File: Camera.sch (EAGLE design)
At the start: 49 parts, among them J1 DM3AT-SF-PEJM5, SW5 THAU13-AB-R, SW6 THAU13-AB-R, SW7 TVAF06-A020B-R, SW8 TVAF06-A020B-R, U4 OPA340N, U5 DRIVER-LV8548MC-AH(SOIC10), U6 I-02247_NJM2845

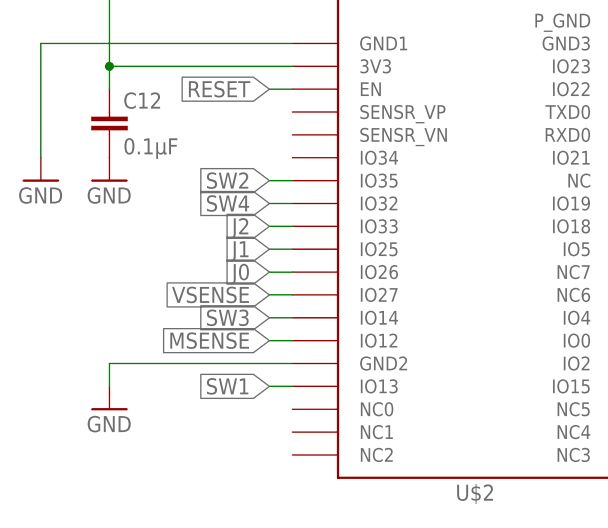
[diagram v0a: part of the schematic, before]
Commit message: Fix analog input pins
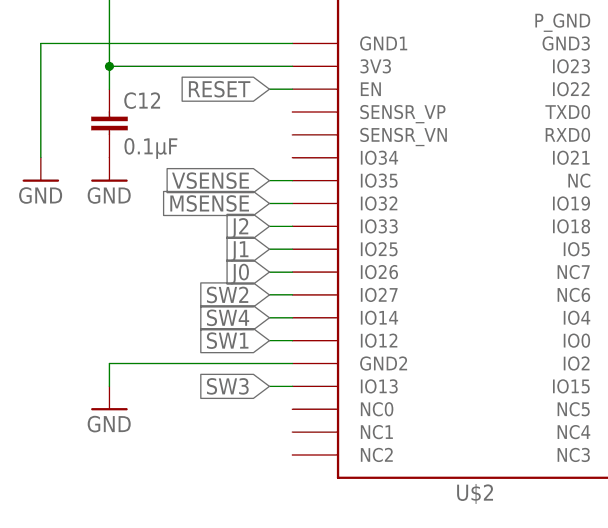
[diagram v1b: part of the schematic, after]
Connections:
- net MSENSE: now also U$2.IO32; no longer U$2.IO12
- net SW1: now also U$2.IO12; no longer U$2.IO13
- net SW2: now also U$2.IO27; no longer U$2.IO35
- net SW3: now also U$2.IO13; no longer U$2.IO14
- net SW4: now also U$2.IO14; no longer U$2.IO32
- net VSENSE: now also U$2.IO35; no longer U$2.IO27
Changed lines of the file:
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@@
 </segment>
 <segment>
-<pinref part="U$2" gate="G$1" pin="IO12"/>
-<wire x1="30.48" y1="17.78" x2="27.94" y2="17.78" width="0.1524" layer="91"/>
-<label x="27.94" y="17.78" size="1.778" layer="95" rot="R180" xref="yes"/>
+<pinref part="U$2" gate="G$1" pin="IO32"/>
+<wire x1="30.48" y1="33.02" x2="27.94" y2="33.02" width="0.1524" layer="91"/>
+<label x="27.94" y="33.02" size="1.778" layer="95" rot="R180" xref="yes"/>
 </segment>
 </net>
@@
 </segment>
 <segment>
-<pinref part="U$2" gate="G$1" pin="IO27"/>
-<wire x1="30.48" y1="22.86" x2="27.94" y2="22.86" width="0.1524" layer="91"/>
-<label x="27.94" y="22.86" size="1.778" layer="95" rot="R180" xref="yes"/>
+<pinref part="U$2" gate="G$1" pin="IO35"/>
+<wire x1="30.48" y1="35.56" x2="27.94" y2="35.56" width="0.1524" layer="91"/>
+<label x="27.94" y="35.56" size="1.778" layer="95" rot="R180" xref="yes"/>
 </segment>
 </net>
@@
 </segment>
 <segment>
-<pinref part="U$2" gate="G$1" pin="IO35"/>
-<wire x1="30.48" y1="35.56" x2="27.94" y2="35.56" width="0.1524" layer="91"/>
-<label x="27.94" y="35.56" size="1.778" layer="95" rot="R180" xref="yes"/>
+<pinref part="U$2" gate="G$1" pin="IO27"/>
+<wire x1="30.48" y1="22.86" x2="27.94" y2="22.86" width="0.1524" layer="91"/>
+<label x="27.94" y="22.86" size="1.778" layer="95" rot="R180" xref="yes"/>
 </segment>
 </net>
@@
 </segment>
 <segment>
+<pinref part="U$2" gate="G$1" pin="IO13"/>
+<wire x1="30.48" y1="12.7" x2="27.94" y2="12.7" width="0.1524" layer="91"/>
+<label x="27.94" y="12.7" size="1.778" layer="95" rot="R180" xref="yes"/>
+</segment>
+</net>
+<net name="SW4" class="0">
+<segment>
+<pinref part="SW8" gate="G$1" pin="A"/>
+<wire x1="218.44" y1="83.82" x2="215.9" y2="83.82" width="0.1524" layer="91"/>
+<label x="215.9" y="83.82" size="1.778" layer="95" rot="R180" xref="yes"/>
+</segment>
+<segment>
 <pinref part="U$2" gate="G$1" pin="IO14"/>
 <wire x1="30.48" y1="20.32" x2="27.94" y2="20.32" width="0.1524" layer="91"/>
@@
 </segment>
 </net>
-<net name="SW4" class="0">
-<segment>
-<pinref part="SW8" gate="G$1" pin="A"/>
-<wire x1="218.44" y1="83.82" x2="215.9" y2="83.82" width="0.1524" layer="91"/>
-<label x="215.9" y="83.82" size="1.778" layer="95" rot="R180" xref="yes"/>
-</segment>
-<segment>
-<pinref part="U$2" gate="G$1" pin="IO32"/>
-<wire x1="30.48" y1="33.02" x2="27.94" y2="33.02" width="0.1524" layer="91"/>
-<label x="27.94" y="33.02" size="1.778" layer="95" rot="R180" xref="yes"/>
-</segment>
-</net>
 <net name="SW1" class="0">
 <segment>
@@
 </segment>
 <segment>
-<pinref part="U$2" gate="G$1" pin="IO13"/>
-<wire x1="30.48" y1="12.7" x2="27.94" y2="12.7" width="0.1524" layer="91"/>
-<label x="27.94" y="12.7" size="1.778" layer="95" rot="R180" xref="yes"/>
-</segment>
-</net>
+<pinref part="U$2" gate="G$1" pin="IO12"/>
+<wire x1="30.48" y1="17.78" x2="27.94" y2="17.78" width="0.1524" layer="91"/>
+<label x="27.94" y="17.78" size="1.778" layer="95" rot="R180" xref="yes"/>
+</segment>
+</net>

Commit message: reduce switch pins
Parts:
- removed C10: 2.2µF, rcl:C-EUC0603
- removed C11: 220µF, rcl:CPOL-EUUD-6,3X7,7
- removed C12, C7: 0.1µF, rcl:C-EUC0603
- removed C8: 1µF, rcl:C-EUC0603
- removed C9: 0.33µF, rcl:C-EUC0603
- removed J1: DM3AT-SF-PEJM5, dm3at-sf-pejm5:DM3AT-SF-PEJM5
- removed J3, J4, J5: (no value), jumper:SJ
- removed R10, R8: 1k, rcl:R-US_R0603
- removed R11, R13, R14, R9: 100k, rcl:R-US_R0603
- removed R12: 200k, rcl:R-US_R0603
- removed U$2: ESP32-WROVER-E, esp32:ESP32-WROVER-E
- removed U$4: SS12D01GX, switches:SS12D01GX
- removed U$5: P2_5_1.27, pins:P2_5_1.27
- added C15, C20: 0.1µF, rcl:C-EUC0603
- added C16: 1µF, rcl:C-EUC0603
- added C17: 0.33µF, rcl:C-EUC0603
- added C18: 2.2µF, rcl:C-EUC0603
- added C19: 220µF, rcl:CPOL-EUUD-6,3X7,7
- added R18, R20: 1k, rcl:R-US_R0603
- added R19, R21, R23, R24: 100k, rcl:R-US_R0603
- added R22: 200k, rcl:R-US_R0603
- added R25, R26, R27, R28, R29: (no value), rcl:R-US_R0603
- added U$7: ESP32-WROVER-E, esp32:ESP32-WROVER-E
- added U$8: SS12D01GX, switches:SS12D01GX
- added U$9: P2_5_1.27, pins:P2_5_1.27
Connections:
- removed net J0: J3.1, U$2.IO26
- removed net J1: J4.1, U$2.IO25
- removed net J2: J5.1, U$2.IO33
- removed net N$10: R14.1, T1.G, U$4.A
- removed net N$5: HUSE1.P2, R14.2, T1.S
- removed net N$8: R8.2, R9.1, U4.-IN
- removed net N$9: R10.2, R11.1, U4.+IN
- removed net SW1: SW6.A, U$2.IO12
- removed net SW2: SW5.A, U$2.IO27
- removed net SW3: SW7.A, U$2.IO13
- removed net SW4: SW8.A, U$2.IO14
- new net N$14: HUSE1.P2, R24.2, T1.S
- new net N$15: R18.2, R19.1, U4.-IN
- new net N$16: R20.2, R21.1, U4.+IN
- new net N$17: R24.1, T1.G, U$8.A
- new net N$20: R27.1, R28.2, SW5.A, SW7.B
- new net N$21: R26.1, R27.2, SW6.B, SW7.A
- new net N$22: R28.1, R29.2, SW5.B, SW8.A
- new net SW: R25.1, R26.2, SW6.A, U$7.IO34
- net 1: now also U$9.7; no longer U$5.7
- net 2: now also U$9.8; no longer U$5.8
- net 3: now also U$9.9; no longer U$5.9
- net 4: now also U$9.10; no longer U$5.10
- net GND: now also C15.2, C16.1, C17.2, C18.2, C19.-, C20.2, R18.1, R21.2, R23.1, R29.1, U$7.GND1, U$7.GND2, U$7.GND3, U$7.P_GND, U$8.C, U$9.2; no longer C10.2, C11.-, C12.2, C7.2, C8.1, C9.2, J3.2, J4.2, J5.2, R11.2, R13.1, R8.1, SW5.B, SW6.B, SW7.B, U$2.GND1, U$2.GND2, U$2.GND3, U$2.P_GND, U$4.C, U$5.2
- net I2C_SCL: now also U$7.IO22; no longer U$2.IO22
- net I2C_SDA: now also U$7.IO21; no longer U$2.IO21
- net LED: now also U$7.IO2; no longer U$2.IO2
- net MC1: now also U$7.IO15; no longer U$2.IO15
- net MC2: now also U$7.IO4; no longer U$2.IO4
- net MGND: now also R20.1; no longer R10.1
- net MSENSE: now also R19.2, U$7.IO32; no longer R9.2, U$2.IO32
- net PRG: now also U$7.IO0, U$9.4; no longer U$2.IO0, U$5.4
- net RESET: now also U$7.EN, U$9.3; no longer U$2.EN, U$5.3
- net RX: now also U$7.RXD0, U$9.6; no longer U$2.RXD0, U$5.6
- net SPI_CLK: now also U$7.IO18; no longer U$2.IO18
- net SPI_CS: now also U$7.IO5; no longer U$2.IO5
- net SPI_MISO: now also U$7.IO19; no longer U$2.IO19
- net TX: now also U$7.TXD0, U$9.5; no longer U$2.TXD0, U$5.5
- net VCC: now also C16.2, C17.1, R22.2; no longer C8.2, C9.1, R12.2
- net VDD: now also C15.1, C18.1, C19.+, C20.1, R25.2, U$7.3V3, U$9.1; no longer C10.1, C11.+, C12.1, C7.1, U$2.3V3, U$5.1
- net VSENSE: now also R22.1, R23.2, U$7.IO35; no longer R12.1, R13.2, U$2.IO35
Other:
- note added: "Limit Switches & Push Switches"
- note removed: "Jumper Pads"
- note removed: "Limit Switches"
- note removed: "Push Switches"
- moved on the sheet: C1, C13, C14, C2, C3, C4, C5, C6, HUSE1, LED4, LED5, LED6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

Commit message: Camera Unit
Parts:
- added C7: 15pF, rcl:C-EUC0603
- added C8: 0.1µF, rcl:C-EUC0603
- added R6: 1k, rcl:R-US_R0603
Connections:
- removed net SPI_CLK: U$7.IO18
- removed net SPI_CS: U$7.IO5
- removed net SPI_MISO: U$7.IO19
- new net CAM_RESET: U$1.RST, U$7.IO14
- new net D0: U$1.D0, U$7.IO5
- new net D1: U$1.D1, U$7.IO19
- new net D2: U$1.D2, U$7.IO23
- new net D3: U$1.D3, U$7.IO18
- new net D4: U$1.D4, U$7.IO27
- new net D5: U$1.D5, U$7.IO33
- new net D6: U$1.D6, U$7.SENSR_VN
- new net D7: U$1.D7, U$7.SENSR_VP
- new net HSYNC: U$1.HREF, U$7.IO26
- new net N$10: U$7.IO13
- new net N$7: R6.1, U$1.PWDN
- new net PCLK: C7.1, U$1.PCLK
- new net VSYNC: U$1.VSYNC, U$7.IO12
- new net XCLK: U$1.XCLK, U$7.IO25
- net GND: now also C7.2, C8.2, R6.2, U$1.AGND, U$1.DGND, U$1.PAD1, U$1.PAD2
- net I2C_SCL: now also U$1.SCL
- net I2C_SDA: now also U$1.SDA
- net VDD: now also C8.1, U$1.DOVDD
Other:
- moved on the sheet: C1, C13, C14, C2, C3, C4, C5, C6, R1, R2, R3, R4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

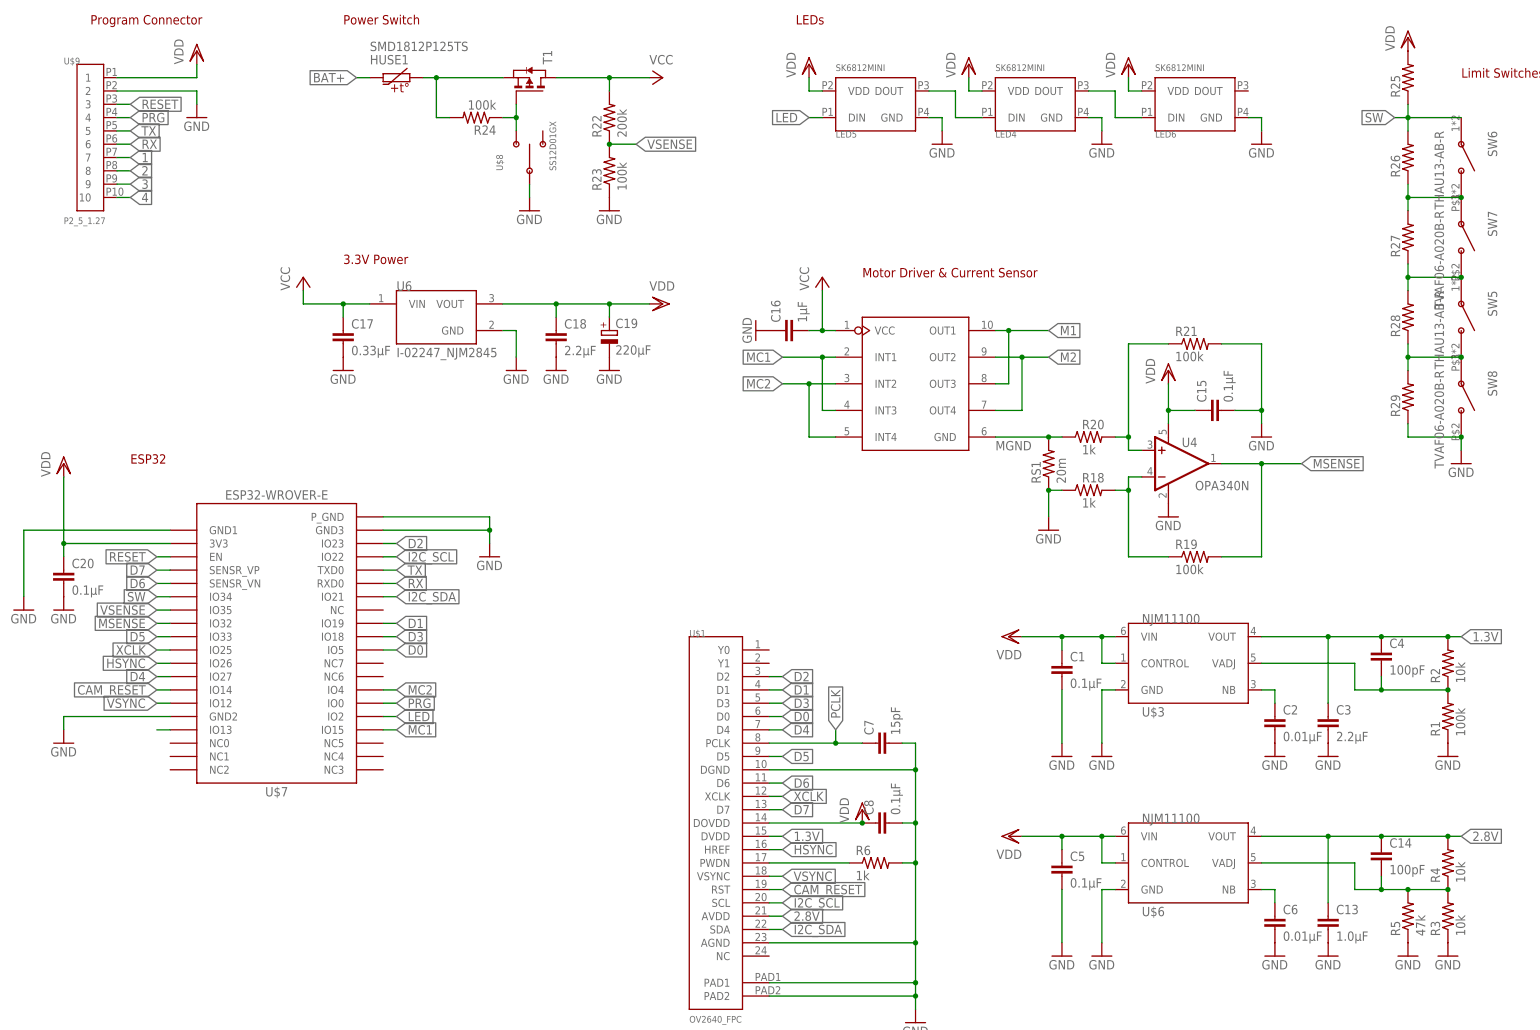
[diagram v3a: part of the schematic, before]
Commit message: change parts name
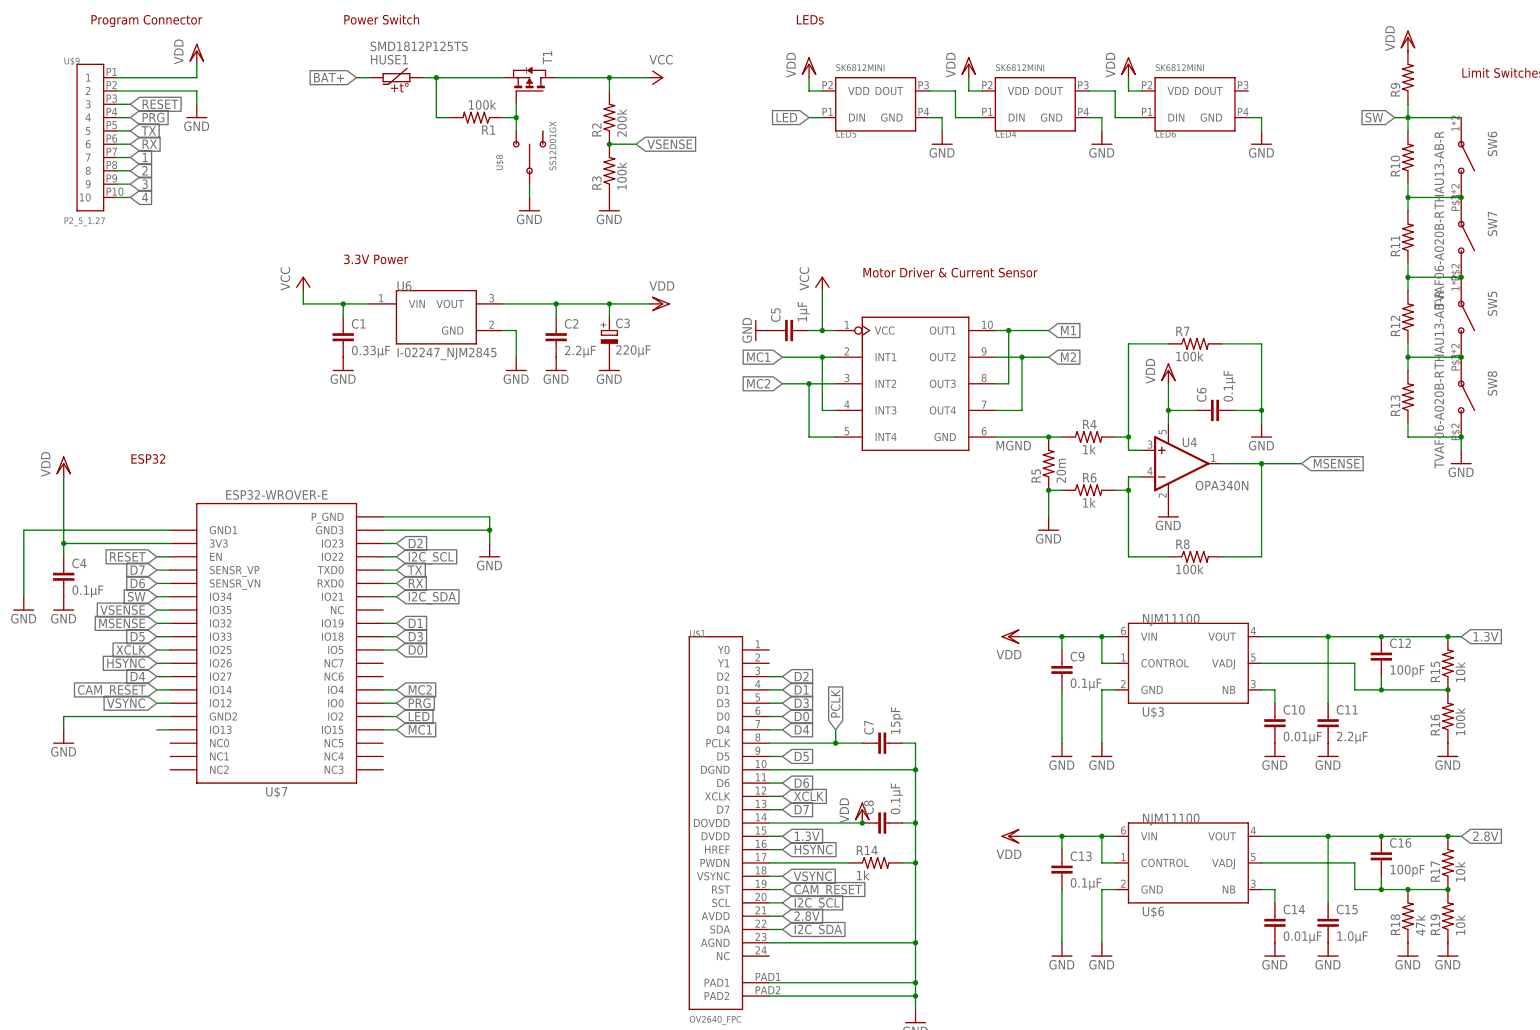
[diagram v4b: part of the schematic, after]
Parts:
- removed C17: 0.33µF, rcl:C-EUC0603
- removed C18: 2.2µF, rcl:C-EUC0603
- removed C19: 220µF, rcl:CPOL-EUUD-6,3X7,7
- removed C20: 0.1µF, rcl:C-EUC0603
- removed R20: 1k, rcl:R-US_R0603
- removed R22: 200k, rcl:R-US_R0603
- removed R23, R24: 100k, rcl:R-US_R0603
- removed RS1: 20m, rcl:R-US_R6332W
- added C10: 0.01µF, resistor:C-EUC0603
- added C11: 2.2µF, resistor:C-EUC0603
- added C12: 100pF, resistor:C-EUC0603
- added C9: 0.1µF, resistor:C-EUC0603
- added R14: 1k, rcl:R-US_R0603
- added R15, R17: 10k, resistor:R-US_R0603
- added R16: 100k, resistor:R-US_R0603
- added R8: 100k, rcl:R-US_R0603
- C1: value 0.1µF -> 0.33µF; device resistor:C-EUC0603 -> rcl:C-EUC0603
- C13: value 1.0µF -> 0.1µF
- C14: value 100pF -> 0.01µF
- C15: value 0.1µF -> 1.0µF; device rcl:C-EUC0603 -> resistor:C-EUC0603
- C16: value 1µF -> 100pF; device rcl:C-EUC0603 -> resistor:C-EUC0603
- C2: value 0.01µF -> 2.2µF; device resistor:C-EUC0603 -> rcl:C-EUC0603
- C3: value 2.2µF -> 220µF; device resistor:C-EUC0603 -> rcl:CPOL-EUUD-6,3X7,7
- C4: value 100pF -> 0.1µF; device resistor:C-EUC0603 -> rcl:C-EUC0603
- C5: value 0.1µF -> 1µF; device resistor:C-EUC0603 -> rcl:C-EUC0603
- C6: value 0.01µF -> 0.1µF; device resistor:C-EUC0603 -> rcl:C-EUC0603
- R1: device resistor:R-US_R0603 -> rcl:R-US_R0603
- R18: value 1k -> 47k; device rcl:R-US_R0603 -> resistor:R-US_R0603
- R19: value 100k -> 10k; device rcl:R-US_R0603 -> resistor:R-US_R0603
- R2: value 10k -> 200k; device resistor:R-US_R0603 -> rcl:R-US_R0603
- R3: value 10k -> 100k; device resistor:R-US_R0603 -> rcl:R-US_R0603
- R4: value 10k -> 1k; device resistor:R-US_R0603 -> rcl:R-US_R0603
- R5: value 47k -> 20m; device resistor:R-US_R0603 -> rcl:R-US_R6332W
- renumbered R21 to R7, R25 to R9, R26 to R10, R27 to R11, R28 to R12, R29 to R13
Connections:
- net 1.3V: now also C11.1, C12.1, R15.2; no longer C3.1, C4.1, R2.2
- net 2.8V: now also C15.1, C16.1, R17.2; no longer C13.1, C14.1, R4.2
- net GND: now also C10.2, C11.2, C14.2, C3.-, C4.2, C5.1, C9.2, R14.2, R16.1, R19.1, R6.1; no longer C16.1, C17.2, C18.2, C19.-, C20.2, C3.2, C5.2, R1.1, R23.1, R6.2, RS1.1
- net MGND: now also R4.1, R5.2; no longer R20.1, RS1.2
- net MSENSE: now also R8.2; no longer R19.2
- net N$1: now also C10.1; no longer C2.1
- net N$14: now also R1.2; no longer R24.2
- net N$15: now also R6.2, R8.1; no longer R18.2, R19.1
- net N$16: now also R4.2; no longer R20.2
- net N$17: now also R1.1; no longer R24.1
- net N$2: now also C12.2, R15.1, R16.2; no longer C4.2, R1.2, R2.1
- net N$3: now also C14.1; no longer C6.1
- net N$4: now also C16.2, R17.1, R18.2, R19.2; no longer C14.2, R3.2, R4.1, R5.2
- net N$7: now also R14.1; no longer R6.1
- net VCC: now also C1.1, C5.2, R2.2; no longer C16.2, C17.1, R22.2
- net VDD: now also C13.1, C2.1, C3.+, C4.1, C6.1, C9.1; no longer C1.1, C15.1, C18.1, C19.+, C20.1, C5.1
- net VSENSE: now also R2.1, R3.2; no longer R22.1, R23.2
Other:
- moved on the sheet: C1, C13, C14, C15, C16, C2, C4, C5, C6, R1, R18, R19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
